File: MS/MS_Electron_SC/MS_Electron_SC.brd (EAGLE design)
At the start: 100 x 80 mm, 44 parts, among them K1 G5LE, K2 G5LE, K3 G5LE, U1 MAX3485CSA

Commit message: More MS dev
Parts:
- added C5, C6: 100nf, OPL_Capacitor:C0805
- added D8: MMSD4148-sod123, OPL_Discrete_Semiconductor:SOD-123
- added D9: RED-0805, OPL_Optoelectronics:LED-0805
- added IC1: MCP23017SO, adafruit:SO28W
- added J4: (no value), SparkFun-Connectors:SCREWTERMINAL-3.5MM-3
- added JP4, JP5, JP6: JUMPER-SMT_3_1-NC_TRACE_SILK, SparkFun-Jumpers:SMT-JUMPER_3_1-NC_TRACE_SILK
- added K4: G5LE, relay:G5LE
- added R11, R12, R13, R14, R15: 1K, OPL_Resistor:R0805
- added U$11: 10K, OPL_Resistor:R0805
- added U$12: MMBT3904LT1G, OPL_Discrete_Semiconductor:SOT-23
- added U2: MCP2515, SparkFun-IC-Comms:SO18W
- added X4: (no value), con-molex-micro-fit-3_0:43045-0600
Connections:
- new net LEDO1: IC1.25, R13.2
- new net LEDO2: IC1.26, R14.2
- new net LEDO3: IC1.27, R15.2
- new net MOSI1: U$1.#27, U$1.27, U$1.@27
- new net N$23: D8.+, D9.-, K4.2, U$12.3
- new net N$24: R11.1, U$11.2, U$12.1
- new net N$25: D9.+, R12.2
- new net N$26: J4.2, K4.P
- new net N$27: J4.1, K4.O
- new net N$28: J4.3, K4.S
- new net N$29: R13.1, X4.P$1
- new net N$30: R14.1, X4.P$3
- new net N$31: IC1.15, JP6.2
- new net N$32: R15.1, X4.P$5
- new net N$33: IC1.16, JP4.2
- new net N$34: IC1.17, JP5.2
- new net RELAY4: IC1.24, R11.2
- new net SCL: IC1.12, U$1.#26, U$1.26, U$1.@26
- new net SDA: IC1.13, U$1.#25, U$1.25, U$1.@25
- net +5V: now also C5.2, IC1.18, IC1.9, JP4.1, JP5.1, JP6.1
- net CAN2_RX: no longer U$1.#27, U$1.27, U$1.@27
- net CAN2_TX: no longer U$1.#26, U$1.26, U$1.@26
- net GND: now also C5.1, C6.1, IC1.10, JP4.3, JP5.3, JP6.3, U$11.1, U$12.2, U2.9, X4.P$2, X4.P$4, X4.P$6
- net RELAY1: now also IC1.21
- net RELAY2: now also IC1.22
- net RELAY3: now also IC1.23
- net VDD: now also C6.2, D8.-, K4.1, R12.1, U2.18

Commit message: Added Isolated CANBUS etc
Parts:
- removed U$2: MCP2551-I/P, Microchip_By_element14_Batch_1:DIP254P762X432-8
- removed X2: (no value), con-molex-micro-fit-3_0:43650-0200
- added C10, C11: 560PF 50V, OPL_Capacitor:C0402
- added C12, C13, C14, C7, C8: 100nf, OPL_Capacitor:C0805
- added C9: (no value), OPL_Capacitor:C1206
- added IC2: ISO1050DUB, texas:DUB-R-PDSO-G8
- added JP7: JUMPER-SMT_3_1-NC_TRACE_SILK, SparkFun-Jumpers:SMT-JUMPER_3_1-NC_TRACE_SILK
- added JP8: JUMPER-SMT_2_NO_SILK, SparkFun-Jumpers:SMT-JUMPER_2_NO_SILK
- added R16, R17: 100, OPL_Resistor:R0805
- added R18: 1M, OPL_Resistor:R0805
- added R19, R20: 4.7k, OPL_Resistor:R0805
- added R21: 120, OPL_Resistor:R0805
- added U$14, U$17: 10K, OPL_Resistor:R0805
- added U3: RFB-0505S, SparkFun-IC-Power:RFB-0505S
- added U4, U5: MCP2551, SparkFun-IC-Comms:SO08
- added X5, X6: (no value), con-molex-micro-fit-3_0:43650-0300
- added Y1: 16MHZ, OPL_Crystal Oscillator:X3-SMD-3.6X1.3X0.8MM
- U$4: value MCP2551-I/P -> 10K; device Microchip_By_element14_Batch_1:DIP254P762X432-8 -> OPL_Resistor:R0805
- X1: device con-molex-micro-fit-3_0:43650-0200 -> con-molex-micro-fit-3_0:43045-0400
- moved U$4 458.5 mm to (-217.2, -364.5)
- moved X1 458.0 mm to (-231.1, -364.5)
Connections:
- new net CAN2_INT: U2.12
- new net CAN2_RST: U$14.2, U2.17
- new net GND-ISO: C10.1, C11.1, C8.1, IC2.5, JP7.3, U3.4
- new net INTB: IC1.19, U$1.#19, U$1.19, U$1.@19
- new net N$35: JP8.2, R21.1
- new net N$36: U$4.2, U5.8
- new net N$37: C10.2, R17.1
- new net N$38: C11.2, R16.1
- new net N$39: R18.1, U2.7, Y1.3
- new net N$40: R18.2, U2.8, Y1.1
- new net N$42: JP7.2, X5.P$1
- new net N$43: U$17.2, U4.8
- new net SWT0: IC1.1
- new net SWT1: IC1.2
- new net SWT2: IC1.3
- new net SWT3: IC1.4
- new net VCC-ISO: C8.2, IC2.8, U3.6
- net +5V: now also C13.2, C14.2, C7.2, C9.2, U3.1, U4.3, U5.3
- net CAN1_RX: now also IC2.2, U5.4; no longer U$2.4
- net CAN1_TX: now also IC2.3, U5.1; no longer U$2.1
- net CAN2_RX: now also U2.2, U4.4; no longer U$4.4
- net CAN2_TX: now also U2.1, U4.1; no longer U$4.1
- net CANH1: now also IC2.7, R16.2, R21.2, R3.2, U5.7, X5.P$2; no longer JP2.1, U$2.7, X1.P$1
- net CANH2: now also R4.2, U4.7, X6.P$2; no longer JP3.1, U$4.7, X2.P$1
- net CANL1: now also IC2.6, JP2.1, JP8.1, R17.2, U5.6, X5.P$3; no longer R3.2, U$2.6, X1.P$2
- net CANL2: now also JP3.1, U4.6, X6.P$3; no longer R4.2, U$4.6, X2.P$2
- net GND: now also C12.1, C13.1, C14.1, C7.1, C9.1, IC2.4, JP7.1, U$17.1, U$4.1, U3.2, U4.2, U5.2, X6.P$1, Y1.2; no longer U$2.2, U$4.2
- net MISO1: now also U2.15
- net MOSI1: now also U2.14
- net SCK1: now also U2.13
- net SCL: now also R19.1
- net SDA: now also R20.1
- net SS1: now also U2.16
- net VDD: now also C12.2, IC2.1, R19.2, R20.2, U$14.1, U4.5, U5.5; no longer U$2.3, U$4.3

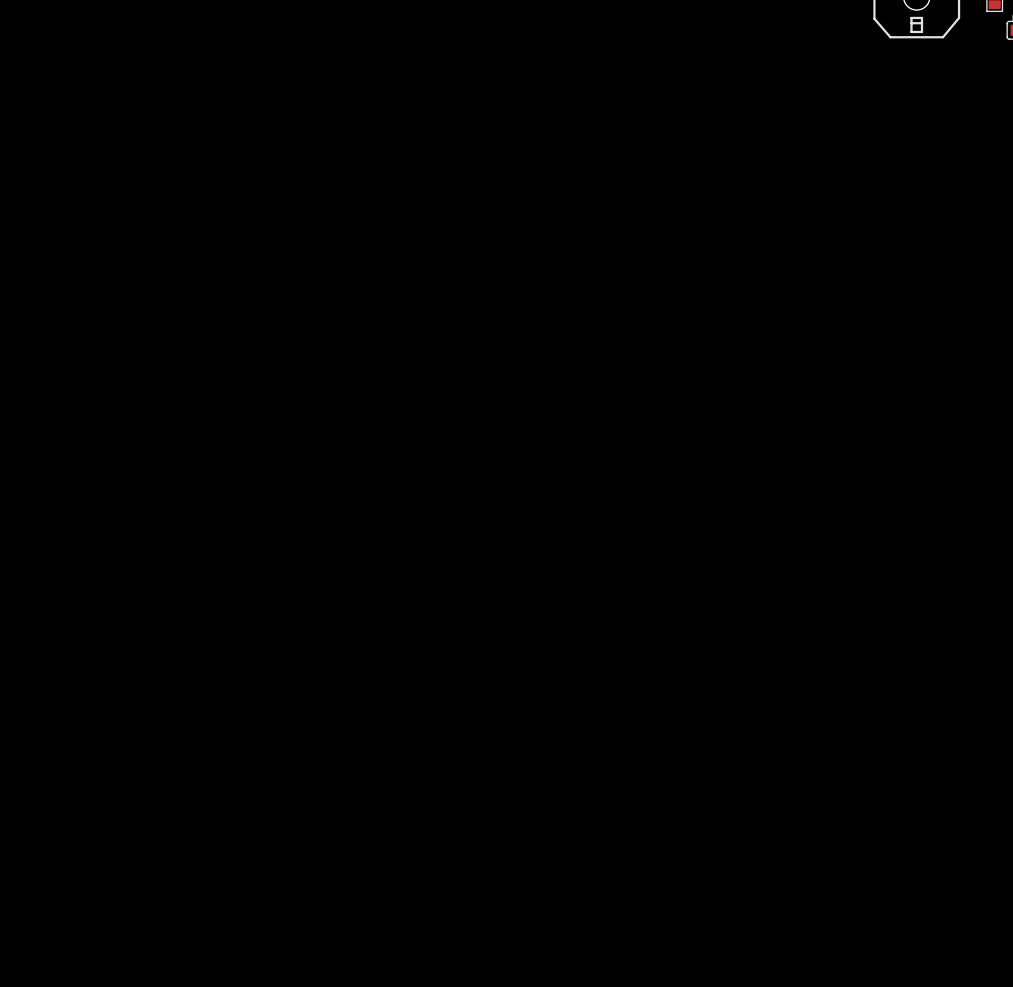
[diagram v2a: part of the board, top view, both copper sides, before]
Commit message: Added datasheets etc
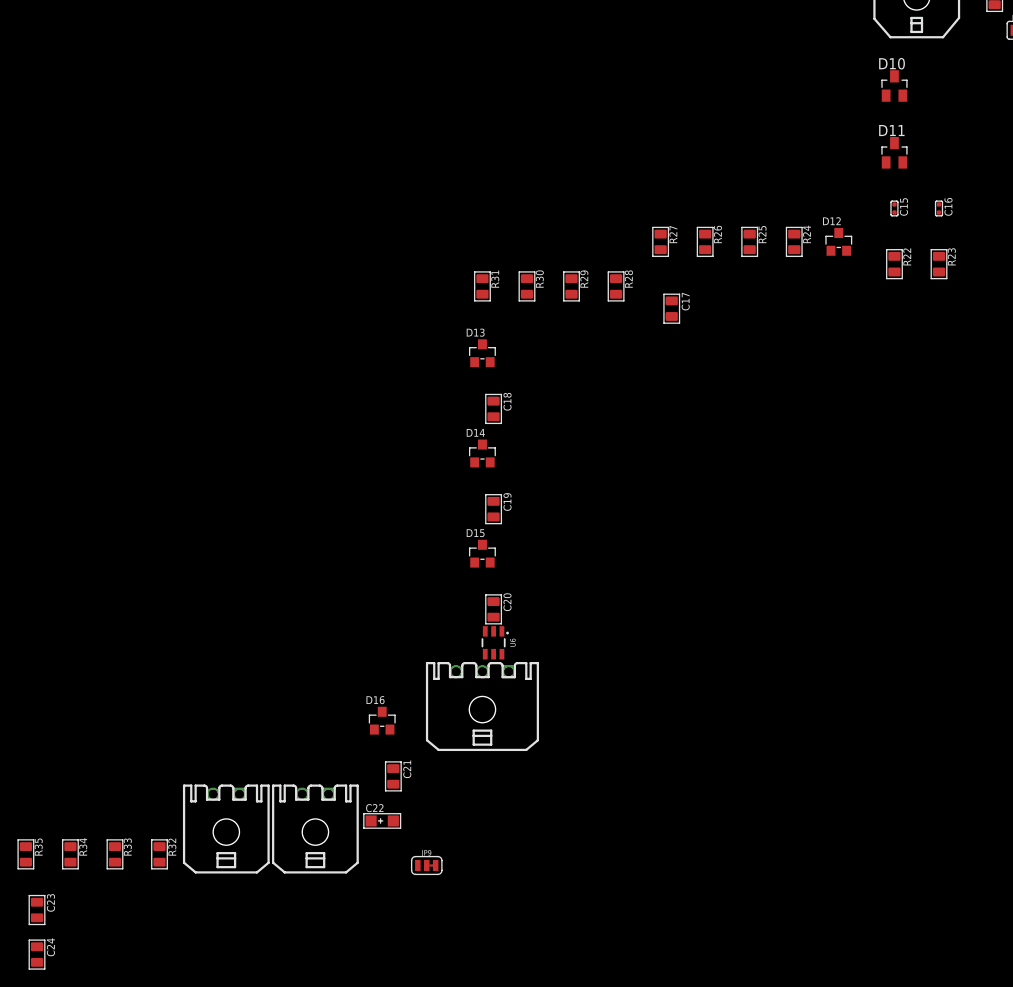
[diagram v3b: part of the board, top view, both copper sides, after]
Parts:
- added C15, C16: 560PF 50V, OPL_Capacitor:C0402
- added C17, C18, C19, C20, C23, C24: 10nf, OPL_Capacitor:C0805
- added C21: 100nf, OPL_Capacitor:C0805
- added C22: 10uf, OPL_Capacitor:AVX-A
- added D10, D11: PESD1CAN, diode:SOT23
- added D12, D13, D14, D15, D16: 5V-225MW, OPL_Circuit_Protection:SOT-23
- added JP9: JUMPER-SMT_3_1-NC_TRACE_SILK, SparkFun-Jumpers:SMT-JUMPER_3_1-NC_TRACE_SILK
- added R22, R23: 100, OPL_Resistor:R0805
- added R24, R25, R26, R27: 1K, OPL_Resistor:R0805
- added R28, R29, R30, R31: 100k, OPL_Resistor:R0805
- added R32, R33: 15k, OPL_Resistor:R0805
- added R34, R35: 2k, OPL_Resistor:R0805
- added U6: MCP4725, SparkFun-IC-Conversion:SOT23-6
- added X2: (no value), con-molex-micro-fit-3_0:43650-0300
- added X7, X8: (no value), con-molex-micro-fit-3_0:43650-0200
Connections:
- new net 5VDAC: D16.3, U6.1, X2.P$2
- new net ADC0: C24.1, R32.1, R35.2, U$1.#12, U$1.12, U$1.@12
- new net ADC1: C23.1, R33.1, R34.2, U$1.#11, U$1.11, U$1.@11
- new net N$41: C10.1, C11.1, D10.3, JP7.2, X5.P$1
- new net N$44: C16.2, R22.1
- new net N$45: R24.1, X1.P$1
- new net N$46: R25.1, X1.P$2
- new net N$47: R26.1, X1.P$3
- new net N$48: R27.1, X1.P$4
- new net N$49: JP9.2, U6.6
- new net N$50: R33.2, X8.P$1
- new net N$51: R32.2, X7.P$1
- net +5V: now also C21.2, C22.-, D12.1, D13.1, D14.1, D15.1, D16.1, JP9.1, R19.2, R20.2, R28.2, R29.2, R30.2, R31.2, U6.3, X2.P$1
- net CANH1: now also D10.1
- net CANH2: now also D11.1, R22.2
- net CANL1: now also D10.2
- net CANL2: now also D11.2, R23.2
- net GND: now also C15.1, C16.1, C17.2, C18.2, C19.2, C20.2, C21.1, C22.+, C23.2, C24.2, D11.3, D12.2, D13.2, D14.2, D15.2, D16.2, JP9.3, R34.1, R35.1, U6.2, X2.P$3, X7.P$2, X8.P$2
- net GND-ISO: no longer C10.1, C11.1
- net N$42: now also C15.2, R23.1; no longer JP7.2, X5.P$1
- net SCL: now also U6.5
- net SDA: now also U6.4
- net SWT0: now also C20.1, D15.3, R24.2, R31.1
- net SWT1: now also C19.1, D14.3, R25.2, R30.1
- net SWT2: now also C18.1, D13.3, R26.2, R29.1
- net SWT3: now also C17.1, D12.3, R27.2, R28.1
- net VDD: no longer R19.2, R20.2

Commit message: Neatened Schematic
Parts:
- moved U$11 308.3 mm to (68.6, 39.9)
- moved R12 306.6 mm to (65.0, 36.8)
- moved R11 301.0 mm to (75.7, 41.4)
- moved D8 298.8 mm to (66.0, 32.8)
- moved IC1 298.1 mm to (62.5, 73.4)
- moved D9 297.5 mm to (71.6, 35.8)
- moved U$12 293.5 mm to (76.2, 34.8)
- moved J4 272.2 mm to (67.8, 3.81)
- moved K4 269.0 mm to (71.4, 18.8), turned to 270 degrees
- moved D1 262.8 mm to (49.8, 42.4)
- moved U$9 259.8 mm to (56.1, 42.9)
- moved R10 254.5 mm to (45.2, 40.6)
- moved D6 246.9 mm to (48.8, 34.5)
- moved D7 241.0 mm to (47.2, 37.6)
- moved U$10 240.2 mm to (56.4, 36.6)
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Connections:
- net N$10: now also J1.1; no longer J1.3
- net N$15: now also J2.3; no longer J2.1
- net N$16: now also J2.1; no longer J2.3
- net N$21: now also J3.3; no longer J3.1
- net N$22: now also J3.1; no longer J3.3
- net N$27: now also J4.3; no longer J4.1
- net N$28: now also J4.1; no longer J4.3
- net N$9: now also J1.3; no longer J1.1

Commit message: Layout started
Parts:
- removed JP8: JUMPER-SMT_2_NO_SILK, SparkFun-Jumpers:SMT-JUMPER_2_NO_SILK
- removed R21: 120, OPL_Resistor:R0805
- removed U$3: MICROSD, adafruit:MICROSD
- added CT1, CT2, CT3: 220UF, OPL_Capacitor:ELECTRO-SMD-C-6MM
- added F1, F2: (no value), adafruit:1812
- added JP10, JP11: (no value), adafruit:1X18-BIG
- added SD1: ST-TF-003A, OPL_Connector:MICRO-SD9+4P-SMD-16.1X14.5X1.85MM
- added X9: (no value), con-molex-micro-fit-3_0:43045-0600
- U$1: value ELECTRON_WITH_STACKABLE_HEADERS -> ELECTRON_WITH_HEADERS; device Particle-Devices:ELECTRON_STACKABLE -> Particle-Devices:ELECTRON
- moved JP9 632.2 mm to (40.9, 77.0), flipped to the bottom, turned to 90 degrees
- moved C22 622.8 mm to (26.4, 76.7), turned to 90 degrees
- moved C21 619.2 mm to (28.7, 77.0), turned to 180 degrees
- moved C20 617.5 mm to (76.5, 70.4), turned to 180 degrees
- moved X2 617.4 mm to (34.5, 85.1), turned to 180 degrees
- moved D16 615.9 mm to (31.5, 77.0), turned to 270 degrees
- moved D15 614.9 mm to (79.5, 70.4), turned to 180 degrees
- moved C19 611.7 mm to (76.5, 74.7), turned to 180 degrees
- moved D14 609.1 mm to (79.5, 74.7), turned to 180 degrees
- moved C18 606.0 mm to (76.5, 79.0), turned to 180 degrees
- moved U6 604.3 mm to (36.6, 77.0), turned to 90 degrees
- moved D13 603.4 mm to (79.5, 79.0), turned to 180 degrees
- moved C23 594.7 mm to (17.8, 12.7)
- moved R28 593.5 mm to (82.5, 83.3), turned to 180 degrees
- moved C24 593.1 mm to (7.11, 13.2)
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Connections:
- removed net VBAT: U$1.#34, U$1.34, U$1.@34
- new net 5V: X9.P$5
- new net GPS_PPS: X9.P$6
- new net N$52: JP11.17, U$1.35
- new net N$53: JP11.16, U$1.34
- new net N$54: F1.1, JP10.1, U$1.1
- net !RE: no longer U$1.#16, U$1.@16
- net +5V: now also CT1.+, CT2.+, CT3.+, D2.-, D4.-, D6.-, D8.-, F1.2, K1.1, K2.1, K3.1, K4.1, R10.1, R12.1, R6.1, R8.1; no longer U$1.#1, U$1.1, U$1.@1
- net ACCEL_INT1: now also JP10.5; no longer U$1.#5, U$1.@5
- net ADC0: no longer U$1.#12, U$1.@12
- net ADC1: no longer U$1.#11, U$1.@11
- net CAN1_RX: no longer U$1.#24, U$1.@24
- net CAN1_TX: no longer U$1.#23, U$1.@23
- net CANH1: no longer R21.2
- net CANL1: no longer JP8.1
- net DAC: no longer U$1.#6, U$1.@6
- net DE: no longer U$1.#17, U$1.@17
- net DI: no longer U$1.#18, U$1.@18
- net GND: now also CT1.-, CT2.-, CT3.-, JP10.2, JP11.15, SD1.6, SD1.G1, SD1.G2, SD1.G3, SD1.G4, X4.P$1, X4.P$3, X9.P$2; no longer U$1.#2, U$1.#33, U$1.@2, U$1.@33, U$3.6, U$3.MT1, U$3.MT2, X4.P$4, X4.P$6
- net GPS_PWR_EN: now also JP11.13, X9.P$1; no longer U$1.#31, U$1.@31
- net GPS_RXD: now also JP10.3, X9.P$3; no longer U$1.#3, U$1.@3
- net GPS_TXD: now also JP10.4, X9.P$4; no longer U$1.#4, U$1.@4
- net INTB: no longer U$1.#19, U$1.@19
- net LEDO1: now also R15.2; no longer R13.2
- net LEDO3: now also R13.2; no longer R15.2
- net MISO: now also JP10.8, SD1.7; no longer U$1.#8, U$1.@8, U$3.7
- net MISO1: no longer U$1.#28, U$1.@28
- net MOSI: now also JP10.7, SD1.3; no longer U$1.#7, U$1.@7, U$3.3
- net MOSI1: no longer U$1.#27, U$1.@27
- net N$29: now also R14.1, X4.P$5; no longer R13.1, X4.P$1
- net N$30: now also R13.1, X4.P$4; no longer R14.1, X4.P$3
- net N$32: now also X4.P$6; no longer X4.P$5
- net N$35: now also F2.1, JP11.18, U$1.36; no longer JP8.2, R21.1
- net RO: no longer U$1.#15, U$1.@15
- net SCK: now also JP10.9, SD1.5; no longer U$1.#9, U$1.@9, U$3.5
- net SCK1: no longer U$1.#29, U$1.@29
- net SCL: now also JP11.8; no longer U$1.#26, U$1.@26
- net SDA: now also JP11.7; no longer U$1.#25, U$1.@25
- net SS: now also SD1.2; no longer U$1.#10, U$1.@10, U$3.2
- net SS1: no longer U$1.#30, U$1.@30
- net VDD: now also F2.2, SD1.4; no longer D2.-, D4.-, D6.-, D8.-, K1.1, K2.1, K3.1, K4.1, R10.1, R12.1, R6.1, R8.1, U$1.#36, U$1.36, U$1.@36, U$3.4
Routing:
- net +5V: track 0.00 -> 258.5 mm, vias 0 -> 2
- net GND: track 0.00 -> 124.0 mm, vias 0 -> 12
- net RELAY1: track 0.00 -> 86.8 mm
- net RELAY2: track 0.00 -> 67.9 mm
- net RELAY3: track 0.00 -> 49.9 mm
- net SCL: track 0.00 -> 41.0 mm
- net SDA: track 0.00 -> 40.2 mm, vias 0 -> 2
- net N$32: track 0.00 -> 39.1 mm
- net N$41: track 0.00 -> 33.8 mm
- net N$29: track 0.00 -> 33.6 mm
- net CANH1: track 0.00 -> 32.3 mm
- net RELAY4: track 0.00 -> 31.9 mm
- net N$30: track 0.00 -> 27.9 mm
- net N$8: track 0.00 -> 26.0 mm
- net SWT0: track 0.00 -> 25.5 mm
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- added copper zone on layer 16, net GND
- added copper zone on layer 16, net GND-ISO
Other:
- board size 100 x 80 mm -> 130 x 90 mm

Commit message: Layout Almost Done
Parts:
- removed CT3: 220UF, OPL_Capacitor:ELECTRO-SMD-C-6MM
- added D17: (no value), adafruit:SMADIODE
- added F3, F4: (no value), adafruit:1812
- added R21: 4k7, OPL_Resistor:R0805
- added X10: (no value), con-molex-micro-fit-3_0:43650-0300
- added X11: (no value), con-molex-micro-fit-3_0:43045-0400
- C10, C11, C15, C16: value 560PF 50V -> 560pf; device OPL_Capacitor:C0402 -> OPL_Capacitor:C0805
- moved X2 51.3 mm to (85.9, 85.1)
- moved C21 45.7 mm to (74.2, 71.9)
- moved C22 45.7 mm to (71.9, 71.6)
- moved D16 45.7 mm to (77.0, 71.9)
- moved JP9 45.7 mm to (86.4, 71.9)
- moved U6 45.7 mm to (82.0, 71.9)
- moved CT2 40.1 mm to (16.0, 27.9)
- moved R18 38.1 mm to (33.8, 59.1)
- moved U2 38.1 mm to (26.7, 55.9)
- moved Y1 38.1 mm to (36.3, 59.1)
- moved U$14 37.9 mm to (19.3, 51.8)
- moved C6 37.6 mm to (16.9, 51.8)
- moved R2 37.2 mm to (68.6, 74.3), turned to 180 degrees
- moved JP1 29.0 mm to (65.5, 74.8), turned to 90 degrees
- moved C24 29.0 mm to (35.1, 20.8)
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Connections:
- removed net 5V: X9.P$5
- removed net N$48 (its old number): R27.1, X1.P$4
- new net 1WIRE: JP11.4, R21.1, U$1.22, X10.P$2
- new net N$47: R25.1, X1.P$4
- new net N$55: D17.A, X3.P$1
- new net N$56: D17.C, F3.1
- new net N$60: F4.2, X11.P$1
- net +5V: now also F3.2, F4.1, R21.2, X10.P$1, X9.P$5; no longer CT3.+, X3.P$1
- net A: now also X11.P$3
- net ADC0: now also JP10.12
- net ADC1: now also JP10.11
- net B: now also X11.P$4
- net CAN2_INT: now also U$1.20
- net GND: now also X10.P$3, X11.P$2; no longer CT3.-
- net LEDO1: now also R13.2; no longer R15.2
- net LEDO3: now also R15.2; no longer R13.2
- net N$37: now also C11.2; no longer C10.2
- net N$38: now also C10.2; no longer C11.2
- net N$42: now also C16.2; no longer C15.2
- net N$44: now also C15.2; no longer C16.2
- net N$45: now also X1.P$2; no longer X1.P$1
- net N$46: now also R27.1, X1.P$1; no longer R25.1, X1.P$2
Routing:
- net +5V: track 258.5 -> 644.3 mm, vias 2 -> 7
- net VDD: track 8.83 -> 288.1 mm, vias 0 -> 3
- net CAN1_RX: track 19.3 -> 73.7 mm, vias 0 -> 1
- net GPS_RXD: track 0.00 -> 49.7 mm
- net CAN1_TX: track 12.7 -> 59.7 mm, vias 0 -> 1
- net INTB: track 0.00 -> 41.1 mm, vias 0 -> 2
- net B: track 0.00 -> 41.0 mm, vias 0 -> 2
- net GPS_TXD: track 0.00 -> 40.9 mm
- net GND: track 124.0 -> 164.8 mm, vias 12 -> 22
- net CAN2_TX: track 0.00 -> 40.5 mm
- net SCL: track 41.0 -> 79.8 mm, vias 0 -> 4
- net N$47: track 0.00 -> 34.7 mm
- net A: track 0.00 -> 34.4 mm, vias 0 -> 2
- net CAN2_RX: track 0.00 -> 34.2 mm
- net ADC1: track 0.00 -> 31.2 mm, vias 0 -> 1
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
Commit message: Almost done layout MS
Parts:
- added D18: SM712, diode:SOT23
- added R36, R37: 10R, OPL_Resistor:R0805
- moved F4 28.7 mm to (28.4, 84.3)
- moved X11 28.7 mm to (38.4, 85.1)
- moved U1 27.1 mm to (56.8, 78.0), turned to 90 degrees
- moved C4 22.9 mm to (54.9, 73.8), turned to 270 degrees
- moved R21 21.6 mm to (65.5, 75.9)
- moved X10 21.5 mm to (67.7, 85.1)
- moved R2 17.2 mm to (51.6, 76.6), turned to 0 degrees
- moved JP1 15.0 mm to (51.6, 80.3)
- moved U$17 0.38 mm to (57.9, 32.3)
- moved R29 0.25 mm to (81.2, 62.7)
- moved R30 0.25 mm to (81.2, 58.4)
- moved R31 0.25 mm to (81.2, 54.1)
- moved C18 0.25 mm to (74.5, 62.7)
- moved C19 0.25 mm to (74.5, 58.4)
- moved C20 0.25 mm to (74.5, 54.1)
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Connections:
- removed net !RE: U$1.16, U1.2
- removed net DE: U$1.17, U1.3
- new net DE|!RE: JP11.2, U$1.20, U1.2, U1.3
- new net N$57: D18.1, R36.2, X11.P$3
- new net N$58: D18.2, R37.1, X11.P$4
- net 1WIRE: now also JP11.1, U$1.19; no longer JP11.4, U$1.22
- net A: now also R36.1; no longer X11.P$3
- net ACCEL_INT1: no longer U$1.5
- net B: now also R37.2; no longer X11.P$4
- net CAN2_INT: now also U$1.5; no longer U$1.20
- net DI: now also JP11.4, U$1.22; no longer U$1.18
- net GND: now also D18.3
- net INTB: now also U$1.18; no longer U$1.19
- net RO: now also JP11.3, U$1.21; no longer U$1.15
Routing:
- net VDD: track 288.1 -> 324.8 mm, vias 3 -> 1
- net B: track 41.0 -> 6.47 mm, vias 2 -> 0
- net A: track 34.4 -> 6.83 mm, vias 2 -> 0
- net DE|!RE: track 0.00 -> 25.8 mm
- net INTB: track 41.1 -> 17.9 mm, vias 2 -> 1
- net DI: track 4.21 -> 26.6 mm
- net +5V: track 644.3 -> 662.9 mm, vias 7 -> 9
- net RO: track 4.21 -> 21.9 mm
- net CAN2_INT: track 0.00 -> 14.4 mm, vias 0 -> 1
- net N$57: track 0.00 -> 13.1 mm
- net 1WIRE: track 17.9 -> 29.8 mm
- net N$58: track 0.00 -> 9.79 mm
- net GND: track 164.8 -> 171.1 mm, vias 22 -> 33
- net SDA: track 69.3 -> 73.6 mm
- net RELAY4: track 44.2 -> 40.5 mm
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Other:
- board text added: "+5V"
- board text added: "1 WIRE"
- board text added: "24V MAX"
- board text added: "5V DAC"
- board text added: "A"
- board text added: "ADC1"
- board text added: "ADC2"
- board text added: "B"
- board text added: "CAN1"
- board text added: "CAN2"
- board text added: "CANH"
- board text added: "CANL"
- board text added: "GND"
- board text added: "GPS"
- board text added: "Isolated"
- board text added: "LEDOut"
- board text added: "NC"
- board text added: "Optional"
- board text added: "PWR"
- board text added: "Particle Electron"
- board text added: "RELAY 1"
- board text added: "RELAY 2"
- board text added: "RELAY 3"
- board text added: "RELAY 4"
- board text added: "RS485"
- board text added: "SIG"
- board text added: "SWTIn"

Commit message: tweaks
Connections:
- net N$31 renamed ADR0
- net N$33 renamed ADR1
- net N$34 renamed ADR2
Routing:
- net GND: track 171.1 -> 165.5 mm
- net VDD: track 324.8 -> 328.1 mm, vias 1 -> 2
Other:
- board text added: "ADR0"
- board text added: "ADR1"
- board text added: "ADR2"
- board text added: "Optional f isolated CAN not used"
